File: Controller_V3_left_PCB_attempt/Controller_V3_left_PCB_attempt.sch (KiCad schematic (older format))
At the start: 25 parts, among them IC1 ATTINY24-SS, J1 BATT, J2 NRF_conn, SW1 SW_PUSH, U1 MAX1811, U2 MAX1595, X2 8MHz

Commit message: placement going as placement goes..
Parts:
- removed J2: NRF_conn, symbol CONN_4X2
- added P1: CONN_5X2, symbol CONN_5X2
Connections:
- wire segments 106 -> 120
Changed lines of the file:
@@
-EESchema Schematic File Version 2  date 14-08-2012 22:19:23
+EESchema Schematic File Version 2  date 15-08-2012 09:24:22
 LIBS:power
 LIBS:device
@@
 LIBS:MAX1595
 LIBS:max1811
+LIBS:Controller_V3_left_PCB_attempt-cache
 EELAYER 25  0
 EELAYER END
@@
 Sheet 1 1
 Title ""
-Date "14 aug 2012"
+Date "15 aug 2012"
 Rev ""
 Comp ""
@@
 Comment4 ""
 $EndDescr
+Connection ~ 7650 2250
+Wire Wire Line
+	8100 2250 7200 2250
+Wire Wire Line
+	8100 2250 8100 2450
+Wire Wire Line
+	8100 2450 8050 2450
+Wire Wire Line
+	7250 2550 7200 2550
+Wire Wire Line
+	7250 2750 7200 2750
+Wire Wire Line
+	7650 3000 7650 3050
+Wire Wire Line
+	8100 2850 8100 3000
+Wire Wire Line
+	8100 2850 8050 2850
+Wire Wire Line
+	8050 2650 8100 2650
 Wire Wire Line
 	1200 5200 1200 5250
@@
 Wire Wire Line
 	2800 3000 2800 3150
-Wire Wire Line
-	8300 2300 8300 2450
-Wire Wire Line
-	6750 2700 6750 2450
 Connection ~ 2600 3550
 Wire Wire Line
 	2800 3550 2350 3550
-Wire Wire Line
-	8300 2450 8050 2450
 Connection ~ 2150 5350
 Wire Wire Line
@@
 	9950 6250 9950 6500
 Wire Wire Line
-	6750 2450 7250 2450
-Wire Wire Line
 	2600 3650 2600 3550
 Wire Wire Line
@@
 Wire Wire Line
 	1200 5450 1200 5500
+Wire Wire Line
+	8100 2550 8050 2550
+Wire Wire Line
+	8100 2750 8050 2750
+Wire Wire Line
+	7250 2850 7200 2850
+Wire Wire Line
+	7200 2850 7200 3000
+Wire Wire Line
+	7200 3000 8100 3000
+Connection ~ 7650 3000
+Wire Wire Line
+	7200 2650 7250 2650
+Wire Wire Line
+	7250 2450 7200 2450
+Wire Wire Line
+	7200 2450 7200 2250
+Wire Wire Line
+	7650 2250 7650 2200
+$Comp
+L CONN_5X2 P1
+U 1 1 502B4E54
+P 7650 2650
+F 0 "P1" H 7650 2950 60  0000 C CNN
+F 1 "CONN_5X2" V 7650 2650 50  0000 C CNN
+	1    7650 2650
+	1    0    0    -1
+$EndComp
 $Comp
 L CONN_2 USB1
@@
 Vchrg
 $Comp
-L GND #PWR01
+L GND #PWR9
 U 1 1 50252716
 P 2600 3650
-F 0 "#PWR01" H 2600 3650 30  0001 C CNN
+F 0 "#PWR9" H 2600 3650 30  0001 C CNN
 F 1 "GND" H 2600 3580 30  0001 C CNN
 	1    2600 3650
@@
 $EndComp
 $Comp
-L +3.3V #PWR02
+L +3.3V #PWR23
 U 1 1 501904C7
 P 9750 5150
-F 0 "#PWR02" H 9750 5110 30  0001 C CNN
+F 0 "#PWR23" H 9750 5110 30  0001 C CNN
 F 1 "+3.3V" H 9750 5260 30  0000 C CNN
 	1    9750 5150
@@
 $EndComp
 $Comp
-L GND #PWR03
+L GND #PWR20
 U 1 1 50190402
 P 8000 1100
-F 0 "#PWR03" H 8000 1100 30  0001 C CNN
+F 0 "#PWR20" H 8000 1100 30  0001 C CNN
 F 1 "GND" H 8000 1030 30  0001 C CNN
 	1    8000 1100
@@
 $EndComp
 $Comp
-L GND #PWR04
+L GND #PWR19
 U 1 1 501903FD
-P 6750 2700
-F 0 "#PWR04" H 6750 2700 30  0001 C CNN
-F 1 "GND" H 6750 2630 30  0001 C CNN
-	1    6750 2700
-	1    0    0    -1
-$EndComp
-$Comp
-L GND #PWR05
+P 7650 3050
+F 0 "#PWR19" H 7650 3050 30  0001 C CNN
+F 1 "GND" H 7650 2980 30  0001 C CNN
+	1    7650 3050
+	1    0    0    -1
+$EndComp
+$Comp
+L GND #PWR16
 U 1 1 501903F3
 P 6100 2450
-F 0 "#PWR05" H 6100 2450 30  0001 C CNN
+F 0 "#PWR16" H 6100 2450 30  0001 C CNN
 F 1 "GND" H 6100 2380 30  0001 C CNN
 	1    6100 2450
@@
 $EndComp
 $Comp
-L GND #PWR06
+L GND #PWR5
 U 1 1 501903E5
 P 2350 2300
-F 0 "#PWR06" H 2350 2300 30  0001 C CNN
+F 0 "#PWR5" H 2350 2300 30  0001 C CNN
 F 1 "GND" H 2350 2230 30  0001 C CNN
 	1    2350 2300
@@
 $EndComp
 $Comp
-L GND #PWR07
+L GND #PWR21
 U 1 1 4FEA19AE
 P 8050 5950
-F 0 "#PWR07" H 8050 5950 30  0001 C CNN
+F 0 "#PWR21" H 8050 5950 30  0001 C CNN
 F 1 "GND" H 8050 5880 30  0001 C CNN
 	1    8050 5950
@@
 approx 3mA@8MHz@3v3
 $Comp
-L +3.3V #PWR08
+L +3.3V #PWR4
 U 1 1 4FE6ECED
 P 2350 1000
-F 0 "#PWR08" H 2350 960 30  0001 C CNN
+F 0 "#PWR4" H 2350 960 30  0001 C CNN
 F 1 "+3.3V" H 2350 1110 30  0000 C CNN
 	1    2350 1000
@@
 $EndComp
 $Comp
-L +5V #PWR09
+L +5V #PWR6
 U 1 1 4FE08C10
 P 2550 6650
-F 0 "#PWR09" H 2550 6740 20  0001 C CNN
+F 0 "#PWR6" H 2550 6740 20  0001 C CNN
 F 1 "+5V" H 2550 6740 30  0000 C CNN
 	1    2550 6650
@@
 $EndComp
 $Comp
-L +3.3V #PWR010
+L +3.3V #PWR18
 U 1 1 4FC72ABF
-P 8300 2300
-F 0 "#PWR010" H 8300 2260 30  0001 C CNN
-F 1 "+3.3V" H 8300 2410 30  0000 C CNN
-	1    8300 2300
-	1    0    0    -1
-$EndComp
-$Comp
-L +3.3V #PWR011
+P 7650 2200
+F 0 "#PWR18" H 7650 2160 30  0001 C CNN
+F 1 "+3.3V" H 7650 2310 30  0000 C CNN
+	1    7650 2200
+	1    0    0    -1
+$EndComp
+$Comp
+L +3.3V #PWR8
 U 1 1 4FC72AB1
 P 2600 2950
-F 0 "#PWR011" H 2600 2910 30  0001 C CNN
+F 0 "#PWR8" H 2600 2910 30  0001 C CNN
 F 1 "+3.3V" H 2600 3060 30  0000 C CNN
 	1    2600 2950
@@
 $EndComp
 $Comp
-L +3.3V #PWR012
+L +3.3V #PWR11
 U 1 1 4FC72AA1
 P 4350 3950
-F 0 "#PWR012" H 4350 3910 30  0001 C CNN
+F 0 "#PWR11" H 4350 3910 30  0001 C CNN
 F 1 "+3.3V" H 4350 4060 30  0000 C CNN
 	1    4350 3950
@@
 $EndComp
 $Comp
-L GND #PWR013
+L GND #PWR12
 U 1 1 4FC72A57
 P 4350 4250
-F 0 "#PWR013" H 4350 4250 30  0001 C CNN
+F 0 "#PWR12" H 4350 4250 30  0001 C CNN
 F 1 "GND" H 4350 4180 30  0001 C CNN
 	1    4350 4250
@@
 	1    0    0    -1
 $EndComp
-Text GLabel 8050 2750 2    60   Input ~ 0
+Text GLabel 8100 2750 2    60   Input ~ 0
 IRQ
-Text GLabel 8050 2650 2    60   Input ~ 0
+Text GLabel 8100 2650 2    60   Input ~ 0
 MOSI
-Text GLabel 8050 2550 2    60   Input ~ 0
+Text GLabel 8100 2550 2    60   Input ~ 0
 CSN
-Text GLabel 7250 2750 0    60   Input ~ 0
+Text GLabel 7200 2750 0    60   Input ~ 0
 MISO
-Text GLabel 7250 2650 0    60   Input ~ 0
+Text GLabel 7200 2650 0    60   Input ~ 0
 SCK
-Text GLabel 7250 2550 0    60   Input ~ 0
+Text GLabel 7200 2550 0    60   Input ~ 0
 CE
 $Comp
-L GND #PWR014
+L GND #PWR17
 U 1 1 4F5F6BBA
 P 7400 6500
-F 0 "#PWR014" H 7400 6500 30  0001 C CNN
+F 0 "#PWR17" H 7400 6500 30  0001 C CNN
 F 1 "GND" H 7400 6430 30  0001 C CNN
 	1    7400 6500
@@
 $EndComp
 $Comp
-L GND #PWR015
+L GND #PWR24
 U 1 1 4F5F6A53
 P 9950 6500
-F 0 "#PWR015" H 9950 6500 30  0001 C CNN
+F 0 "#PWR24" H 9950 6500 30  0001 C CNN
 F 1 "GND" H 9950 6430 30  0001 C CNN
 	1    9950 6500
@@
 $EndComp
 $Comp
-L GND #PWR016
+L GND #PWR22
 U 1 1 4F5F6856
 P 9700 5950
-F 0 "#PWR016" H 9700 5950 30  0001 C CNN
+F 0 "#PWR22" H 9700 5950 30  0001 C CNN
 F 1 "GND" H 9700 5880 30  0001 C CNN
 	1    9700 5950
 	1    0    0    -1
 $EndComp
-Text Notes 7250 2150 0    60   ~ 0
+Text Notes 7250 2050 0    60   ~ 0
 To wireless module\n
 Text Notes 2950 6050 0    60   ~ 0
@@
 $EndComp
 $Comp
-L +5V #PWR017
+L +5V #PWR3
 U 1 1 4F4F395E
 P 2150 5300
-F 0 "#PWR017" H 2150 5390 20  0001 C CNN
+F 0 "#PWR3" H 2150 5390 20  0001 C CNN
 F 1 "+5V" H 2150 5390 30  0000 C CNN
 	1    2150 5300
@@
 $EndComp
 $Comp
-L +5V #PWR018
+L +5V #PWR13
 U 1 1 4F4F393F
 P 4450 6600
-F 0 "#PWR018" H 4450 6690 20  0001 C CNN
+F 0 "#PWR13" H 4450 6690 20  0001 C CNN
 F 1 "+5V" H 4450 6690 30  0000 C CNN
 	1    4450 6600
@@
 $EndComp
 $Comp
-L GND #PWR019
+L GND #PWR14
 U 1 1 4F4F3934
 P 4450 7300
-F 0 "#PWR019" H 4450 7300 30  0001 C CNN
+F 0 "#PWR14" H 4450 7300 30  0001 C CNN
 F 1 "GND" H 4450 7230 30  0001 C CNN
 	1    4450 7300
@@
 $EndComp
 $Comp
-L GND #PWR020
+L GND #PWR10
 U 1 1 4F4F38CA
 P 4000 7100
-F 0 "#PWR020" H 4000 7100 30  0001 C CNN
+F 0 "#PWR10" H 4000 7100 30  0001 C CNN
 F 1 "GND" H 4000 7030 30  0001 C CNN
 	1    4000 7100
@@
 $EndComp
 $Comp
-L GND #PWR021
+L GND #PWR7
 U 1 1 4F4F38C1
 P 2550 7100
-F 0 "#PWR021" H 2550 7100 30  0001 C CNN
+F 0 "#PWR7" H 2550 7100 30  0001 C CNN
 F 1 "GND" H 2550 7030 30  0001 C CNN
 	1    2550 7100
@@
 $EndComp
 $Comp
-L GND #PWR022
+L GND #PWR15
 U 1 1 4F4F372C
 P 5700 7150
-F 0 "#PWR022" H 5700 7150 30  0001 C CNN
+F 0 "#PWR15" H 5700 7150 30  0001 C CNN
 F 1 "GND" H 5700 7080 30  0001 C CNN
 	1    5700 7150
@@
 $EndComp
 $Comp
-L GND #PWR023
+L GND #PWR2
 U 1 1 4F4F36B2
 P 1200 5500
-F 0 "#PWR023" H 1200 5500 30  0001 C CNN
+F 0 "#PWR2" H 1200 5500 30  0001 C CNN
 F 1 "GND" H 1200 5430 30  0001 C CNN
 	1    1200 5500
@@
 $EndComp
 $Comp
-L +5V #PWR024
+L +5V #PWR1
 U 1 1 4F4F36A7
 P 1200 5200
-F 0 "#PWR024" H 1200 5290 20  0001 C CNN
+F 0 "#PWR1" H 1200 5290 20  0001 C CNN
 F 1 "+5V" H 1200 5290 30  0000 C CNN
 	1    1200 5200
@@
 	0    1    1    0
 $EndComp
-$Comp
-L CONN_4X2 J2
-U 1 1 4F4F3414
-P 7650 2600
-F 0 "J2" H 7650 2850 50  0000 C CNN
-F 1 "NRF_conn" V 7650 2600 40  0000 C CNN
-	1    7650 2600
-	1    0    0    -1
-$EndComp
 $EndSCHEMATC

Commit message: routed some more, Most important change is that switch and battery share a connection on the board
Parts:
- removed D1: LED, symbol LED
- removed J1: BATT, symbol CONN_2
- removed SW1: SW_PUSH, symbol SW_PUSH
- added LED1: CONN_2, symbol CONN_2
- added TOP1: CONN_3, symbol CONN_3
- renumbered P1 to NRF1
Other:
- note added: "Battery_and switchconnector:"
- note added: "batt+ and sw pin 1"
- note added: "batt-"
- note added: "sw pin2"
- note removed: "Battery_connector:"
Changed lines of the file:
@@
-EESchema Schematic File Version 2  date 15-08-2012 09:24:22
+EESchema Schematic File Version 2  date 17-08-2012 09:39:53
 LIBS:power
 LIBS:device
@@
 Sheet 1 1
 Title ""
-Date "15 aug 2012"
+Date "17 aug 2012"
 Rev ""
 Comp ""
@@
 Comment4 ""
 $EndDescr
+Wire Wire Line
+	2150 6250 2150 6500
+Wire Wire Line
+	2150 6250 2100 6250
+Wire Wire Line
+	7300 6700 5700 6700
+Wire Wire Line
+	7300 6800 7000 6800
 Connection ~ 7650 2250
 Wire Wire Line
@@
 	7250 2750 7200 2750
 Wire Wire Line
-	7650 3000 7650 3050
+	7650 3050 7650 3000
 Wire Wire Line
 	8100 2850 8100 3000
@@
 	1200 5250 1150 5250
 Wire Wire Line
-	5700 6450 5700 6700
-Connection ~ 6550 6700
-Wire Wire Line
-	6550 6700 6550 6450
-Wire Wire Line
-	6550 6450 6600 6450
-Wire Wire Line
-	6500 6700 6650 6700
+	5700 6700 5700 6450
 Wire Wire Line
 	4350 4250 4350 4200
@@
 	2150 5350 2700 5350
 Wire Wire Line
-	2700 6500 2150 6500
-Wire Wire Line
-	2150 6500 2150 6350
+	2150 6500 2700 6500
 Wire Wire Line
 	2150 5300 2150 5400
@@
 Connection ~ 4450 6700
 Wire Wire Line
-	2150 5900 2150 5950
-Wire Wire Line
 	2700 5350 2700 6400
 Wire Wire Line
@@
 	4350 4000 4350 3950
 Wire Wire Line
-	5700 6700 5900 6700
-Wire Wire Line
-	5700 6900 6650 6900
-Wire Wire Line
 	4050 6400 3900 6400
 Wire Wire Line
@@
 	7200 2450 7200 2250
 Wire Wire Line
-	7650 2250 7650 2200
-$Comp
-L CONN_5X2 P1
+	7650 2200 7650 2250
+Wire Wire Line
+	5700 6900 7300 6900
+Wire Wire Line
+	2150 5900 2150 6050
+Wire Wire Line
+	2150 6050 2100 6050
+$Comp
+L CONN_2 LED1
+U 1 1 502DF4BC
+P 1750 6150
+F 0 "LED1" V 1700 6150 40  0000 C CNN
+F 1 "CONN_2" V 1800 6150 40  0000 C CNN
+	1    1750 6150
+	-1   0    0    1
+$EndComp
+Text Notes 7800 6750 0    60   ~ 0
+sw pin2
+Text Notes 7800 6850 0    60   ~ 0
+batt+ and sw pin 1
+Text Notes 7800 6950 0    60   ~ 0
+batt-
+$Comp
+L CONN_3 TOP1
+U 1 1 502DF402
+P 7650 6800
+F 0 "TOP1" V 7600 6800 50  0000 C CNN
+F 1 "CONN_3" V 7700 6800 40  0000 C CNN
+	1    7650 6800
+	1    0    0    -1
+$EndComp
+$Comp
+L CONN_5X2 NRF1
 U 1 1 502B4E54
 P 7650 2650
-F 0 "P1" H 7650 2950 60  0000 C CNN
+F 0 "NRF1" H 7650 2950 60  0000 C CNN
 F 1 "CONN_5X2" V 7650 2650 50  0000 C CNN
 	1    7650 2650
@@
 Vchrg
 $Comp
-L GND #PWR9
+L GND #PWR01
 U 1 1 50252716
 P 2600 3650
-F 0 "#PWR9" H 2600 3650 30  0001 C CNN
+F 0 "#PWR01" H 2600 3650 30  0001 C CNN
 F 1 "GND" H 2600 3580 30  0001 C CNN
 	1    2600 3650
@@
 Text GLabel 5700 6450 1    60   Input ~ 0
 V_Batt_switched
-Text GLabel 6600 6450 2    60   Input ~ 0
+Text GLabel 7000 6800 0    60   Input ~ 0
 Vchrg
 Text GLabel 4050 6400 2    60   Input ~ 0
 Vchrg
-$Comp
-L SW_PUSH SW1
-U 1 1 50192F7D
-P 6200 6700
-F 0 "SW1" H 6350 6810 50  0000 C CNN
-F 1 "SW_PUSH" H 6200 6620 50  0000 C CNN
-	1    6200 6700
-	-1   0    0    -1
-$EndComp
 Text GLabel 4400 4100 2    60   Input ~ 0
 N64Serial
@@
 $EndComp
 $Comp
-L +3.3V #PWR23
+L +3.3V #PWR02
 U 1 1 501904C7
 P 9750 5150
-F 0 "#PWR23" H 9750 5110 30  0001 C CNN
+F 0 "#PWR02" H 9750 5110 30  0001 C CNN
 F 1 "+3.3V" H 9750 5260 30  0000 C CNN
 	1    9750 5150
@@
 $EndComp
 $Comp
-L GND #PWR20
+L GND #PWR03
 U 1 1 50190402
 P 8000 1100
-F 0 "#PWR20" H 8000 1100 30  0001 C CNN
+F 0 "#PWR03" H 8000 1100 30  0001 C CNN
 F 1 "GND" H 8000 1030 30  0001 C CNN
 	1    8000 1100
@@
 $EndComp
 $Comp
-L GND #PWR19
+L GND #PWR04
 U 1 1 501903FD
 P 7650 3050
-F 0 "#PWR19" H 7650 3050 30  0001 C CNN
+F 0 "#PWR04" H 7650 3050 30  0001 C CNN
 F 1 "GND" H 7650 2980 30  0001 C CNN
 	1    7650 3050
@@
 $EndComp
 $Comp
-L GND #PWR16
+L GND #PWR05
 U 1 1 501903F3
 P 6100 2450
-F 0 "#PWR16" H 6100 2450 30  0001 C CNN
+F 0 "#PWR05" H 6100 2450 30  0001 C CNN
 F 1 "GND" H 6100 2380 30  0001 C CNN
 	1    6100 2450
@@
 $EndComp
 $Comp
-L GND #PWR5
+L GND #PWR06
 U 1 1 501903E5
 P 2350 2300
-F 0 "#PWR5" H 2350 2300 30  0001 C CNN
+F 0 "#PWR06" H 2350 2300 30  0001 C CNN
 F 1 "GND" H 2350 2230 30  0001 C CNN
 	1    2350 2300
@@
 $EndComp
 $Comp
-L GND #PWR21
+L GND #PWR07
 U 1 1 4FEA19AE
 P 8050 5950
-F 0 "#PWR21" H 8050 5950 30  0001 C CNN
+F 0 "#PWR07" H 8050 5950 30  0001 C CNN
 F 1 "GND" H 8050 5880 30  0001 C CNN
 	1    8050 5950
@@
 approx 3mA@8MHz@3v3
 $Comp
-L +3.3V #PWR4
+L +3.3V #PWR08
 U 1 1 4FE6ECED
 P 2350 1000
-F 0 "#PWR4" H 2350 960 30  0001 C CNN
+F 0 "#PWR08" H 2350 960 30  0001 C CNN
 F 1 "+3.3V" H 2350 1110 30  0000 C CNN
 	1    2350 1000
@@
 $EndComp
 $Comp
-L +5V #PWR6
+L +5V #PWR09
 U 1 1 4FE08C10
 P 2550 6650
-F 0 "#PWR6" H 2550 6740 20  0001 C CNN
+F 0 "#PWR09" H 2550 6740 20  0001 C CNN
 F 1 "+5V" H 2550 6740 30  0000 C CNN
 	1    2550 6650
@@
 $EndComp
 $Comp
-L +3.3V #PWR18
+L +3.3V #PWR010
 U 1 1 4FC72ABF
 P 7650 2200
-F 0 "#PWR18" H 7650 2160 30  0001 C CNN
+F 0 "#PWR010" H 7650 2160 30  0001 C CNN
 F 1 "+3.3V" H 7650 2310 30  0000 C CNN
 	1    7650 2200
@@
 $EndComp
 $Comp
-L +3.3V #PWR8
+L +3.3V #PWR011
 U 1 1 4FC72AB1
 P 2600 2950
-F 0 "#PWR8" H 2600 2910 30  0001 C CNN
+F 0 "#PWR011" H 2600 2910 30  0001 C CNN
 F 1 "+3.3V" H 2600 3060 30  0000 C CNN
 	1    2600 2950
@@
 $EndComp
 $Comp
-L +3.3V #PWR11
+L +3.3V #PWR012
 U 1 1 4FC72AA1
 P 4350 3950
-F 0 "#PWR11" H 4350 3910 30  0001 C CNN
+F 0 "#PWR012" H 4350 3910 30  0001 C CNN
 F 1 "+3.3V" H 4350 4060 30  0000 C CNN
 	1    4350 3950
@@
 $EndComp
 $Comp
-L GND #PWR12
+L GND #PWR013
 U 1 1 4FC72A57
 P 4350 4250
-F 0 "#PWR12" H 4350 4250 30  0001 C CNN
+F 0 "#PWR013" H 4350 4250 30  0001 C CNN
 F 1 "GND" H 4350 4180 30  0001 C CNN
 	1    4350 4250
@@
 CE
 $Comp
-L GND #PWR17
+L GND #PWR014
 U 1 1 4F5F6BBA
 P 7400 6500
-F 0 "#PWR17" H 7400 6500 30  0001 C CNN
+F 0 "#PWR014" H 7400 6500 30  0001 C CNN
 F 1 "GND" H 7400 6430 30  0001 C CNN
 	1    7400 6500
@@
 $EndComp
 $Comp
-L GND #PWR24
+L GND #PWR015
 U 1 1 4F5F6A53
 P 9950 6500
-F 0 "#PWR24" H 9950 6500 30  0001 C CNN
+F 0 "#PWR015" H 9950 6500 30  0001 C CNN
 F 1 "GND" H 9950 6430 30  0001 C CNN
 	1    9950 6500
@@
 $EndComp
 $Comp
-L GND #PWR22
+L GND #PWR016
 U 1 1 4F5F6856
 P 9700 5950
-F 0 "#PWR22" H 9700 5950 30  0001 C CNN
+F 0 "#PWR016" H 9700 5950 30  0001 C CNN
 F 1 "GND" H 9700 5880 30  0001 C CNN
 	1    9700 5950
@@
 Charging curcuit:\n
 Text Notes 6400 7050 0    60   ~ 0
-Battery_connector:
+Battery_and switchconnector:
 Text GLabel 2050 6450 0    60   Input ~ 0
 CHARGE_INDICATOR
-$Comp
-L LED D1
-U 1 1 4F4F3974
-P 2150 6150
-F 0 "D1" H 2150 6250 50  0000 C CNN
-F 1 "LED" H 2150 6050 50  0000 C CNN
-	1    2150 6150
-	0    1    1    0
-$EndComp
 $Comp
 L R R1
@@
 $EndComp
 $Comp
-L +5V #PWR3
+L +5V #PWR017
 U 1 1 4F4F395E
 P 2150 5300
-F 0 "#PWR3" H 2150 5390 20  0001 C CNN
+F 0 "#PWR017" H 2150 5390 20  0001 C CNN
 F 1 "+5V" H 2150 5390 30  0000 C CNN
 	1    2150 5300
@@
 $EndComp
 $Comp
-L +5V #PWR13
+L +5V #PWR018
 U 1 1 4F4F393F
 P 4450 6600
-F 0 "#PWR13" H 4450 6690 20  0001 C CNN
+F 0 "#PWR018" H 4450 6690 20  0001 C CNN
 F 1 "+5V" H 4450 6690 30  0000 C CNN
 	1    4450 6600
@@
 $EndComp
 $Comp
-L GND #PWR14
+L GND #PWR019
 U 1 1 4F4F3934
 P 4450 7300
-F 0 "#PWR14" H 4450 7300 30  0001 C CNN
+F 0 "#PWR019" H 4450 7300 30  0001 C CNN
 F 1 "GND" H 4450 7230 30  0001 C CNN
 	1    4450 7300
@@
 $EndComp
 $Comp
-L GND #PWR10
+L GND #PWR020
 U 1 1 4F4F38CA
 P 4000 7100
-F 0 "#PWR10" H 4000 7100 30  0001 C CNN
+F 0 "#PWR020" H 4000 7100 30  0001 C CNN
 F 1 "GND" H 4000 7030 30  0001 C CNN
 	1    4000 7100
@@
 $EndComp
 $Comp
-L GND #PWR7
+L GND #PWR021
 U 1 1 4F4F38C1
 P 2550 7100
-F 0 "#PWR7" H 2550 7100 30  0001 C CNN
+F 0 "#PWR021" H 2550 7100 30  0001 C CNN
 F 1 "GND" H 2550 7030 30  0001 C CNN
 	1    2550 7100
@@
 $EndComp
 $Comp
-L GND #PWR15
+L GND #PWR022
 U 1 1 4F4F372C
 P 5700 7150
-F 0 "#PWR15" H 5700 7150 30  0001 C CNN
+F 0 "#PWR022" H 5700 7150 30  0001 C CNN
 F 1 "GND" H 5700 7080 30  0001 C CNN
 	1    5700 7150
@@
 $EndComp
 $Comp
-L CONN_2 J1
-U 1 1 4F4F3715
-P 7000 6800
-F 0 "J1" V 6950 6800 40  0000 C CNN
-F 1 "BATT" V 7050 6800 40  0000 C CNN
-	1    7000 6800
-	1    0    0    -1
-$EndComp
-$Comp
-L GND #PWR2
+L GND #PWR023
 U 1 1 4F4F36B2
 P 1200 5500
-F 0 "#PWR2" H 1200 5500 30  0001 C CNN
+F 0 "#PWR023" H 1200 5500 30  0001 C CNN
 F 1 "GND" H 1200 5430 30  0001 C CNN
 	1    1200 5500
@@
 $EndComp
 $Comp
-L +5V #PWR1
+L +5V #PWR024
 U 1 1 4F4F36A7
 P 1200 5200
-F 0 "#PWR1" H 1200 5290 20  0001 C CNN
+F 0 "#PWR024" H 1200 5290 20  0001 C CNN
 F 1 "+5V" H 1200 5290 30  0000 C CNN
 	1    1200 5200

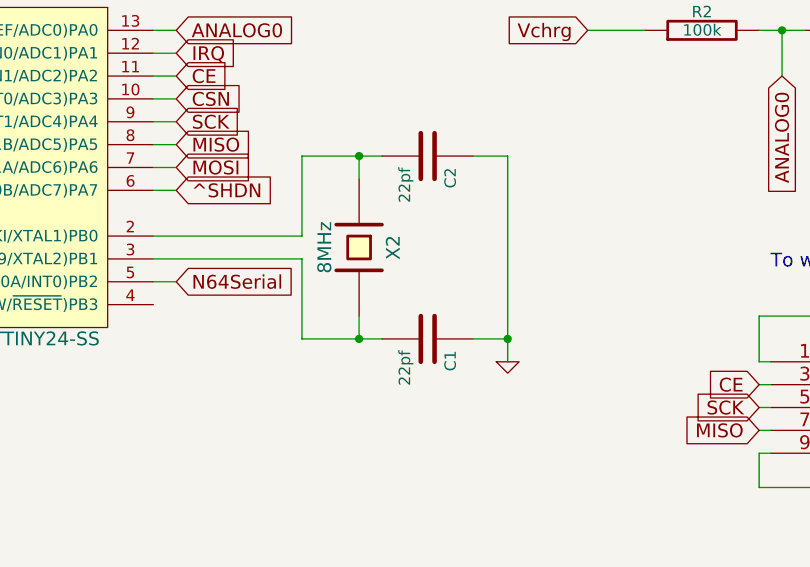
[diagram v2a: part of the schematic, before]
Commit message: pretty final, changed load capacitance on XTAL
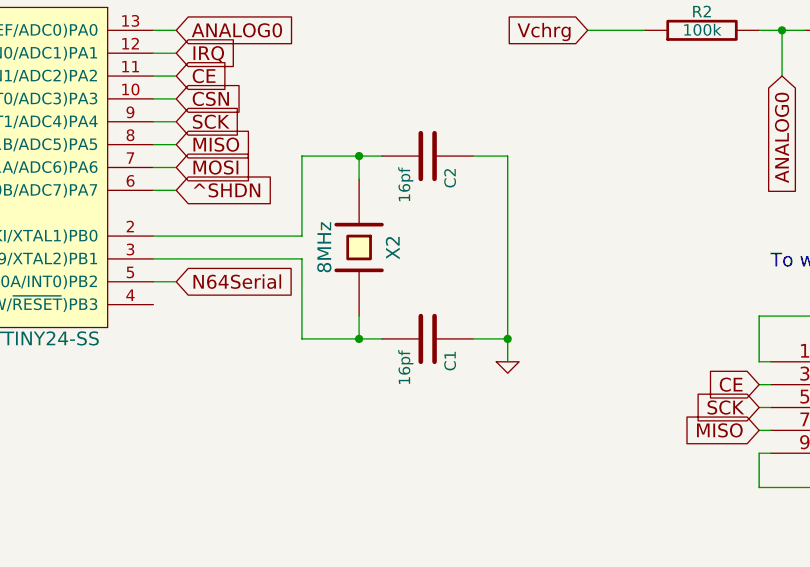
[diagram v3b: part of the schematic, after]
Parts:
- C1, C2: value 22pf -> 16pf
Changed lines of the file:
@@
-EESchema Schematic File Version 2  date 17-08-2012 09:39:53
+EESchema Schematic File Version 2  date 21-08-2012 09:27:37
 LIBS:power
 LIBS:device
@@
 Sheet 1 1
 Title ""
-Date "17 aug 2012"
+Date "21 aug 2012"
 Rev ""
 Comp ""
@@
 P 5750 1550
 F 0 "C2" H 5800 1650 50  0000 L CNN
-F 1 "22pf" H 5800 1450 50  0000 L CNN
+F 1 "16pf" H 5800 1450 50  0000 L CNN
 	1    5750 1550
 	0    1    1    0
@@
 P 5750 2350
 F 0 "C1" H 5800 2450 50  0000 L CNN
-F 1 "22pf" H 5800 2250 50  0000 L CNN
+F 1 "16pf" H 5800 2250 50  0000 L CNN
 	1    5750 2350
 	0    1    1    0

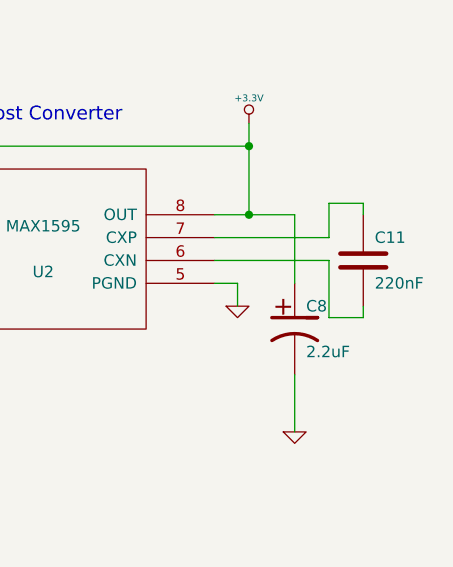
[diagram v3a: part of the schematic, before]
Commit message: corrected value of C11
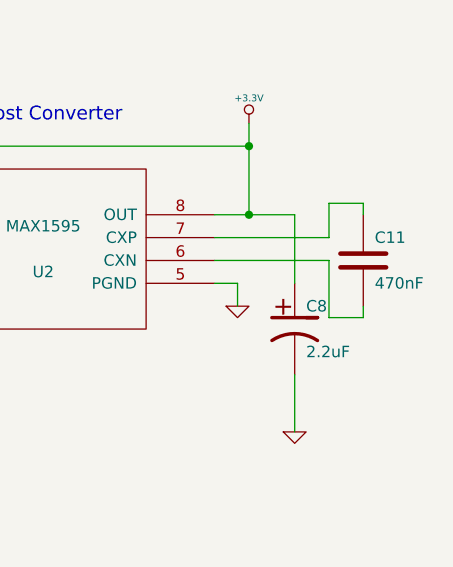
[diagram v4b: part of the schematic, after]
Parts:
- C11: value 220nF -> 470nF
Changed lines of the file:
@@
-EESchema Schematic File Version 2  date 21-08-2012 09:27:37
+EESchema Schematic File Version 2  date 10-10-2012 09:57:18
 LIBS:power
 LIBS:device
@@
 Sheet 1 1
 Title ""
-Date "21 aug 2012"
+Date "10 oct 2012"
 Rev ""
 Comp ""
@@
 P 10250 5750
 F 0 "C11" H 10300 5850 50  0000 L CNN
-F 1 "220nF" H 10300 5650 50  0000 L CNN
+F 1 "470nF" H 10300 5650 50  0000 L CNN
 	1    10250 5750
 	1    0    0    -1
